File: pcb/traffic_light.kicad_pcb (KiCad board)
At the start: 2 copper layers, 30 x 130 mm, 53 parts, among them J2 Power, Q1 BS170, Q2 BS170, Q3 BS170, SW1 RESET, SW2 FLASH, U1 ESP-12F, U2 AMS1117-3.3

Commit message: laying out PCB
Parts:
- removed the REF** at (65.0, 70.0)
- removed the REF** at (65.0, 155.0)
- removed the REF** at (65.0, 77.0)
- added REF**: 1pin, istrukov:1pin_no_outline, F.Cu at (67.8, 70.0)
- added REF**: 1pin, istrukov:1pin_no_outline, F.Cu at (67.5, 155.0)
- added REF**: 1pin, istrukov:1pin_no_outline, F.Cu at (67.5, 77.0)
- moved R7 59.0 mm to (35.9, 112.0)
- moved R8 50.8 mm to (55.8, 110.8), turned to 90 degrees
- moved R12 50.0 mm to (55.8, 121.0)
- moved Q3 23.8 mm to (80.8, 169.6), turned to 90 degrees
- moved R5 23.3 mm to (54.4, 63.4), turned to 0 degrees
- moved R6 23.1 mm to (54.4, 57.4), turned to 0 degrees
- moved Q1 9.40 mm to (81.2, 61.2)
- moved R1 6.88 mm to (81.4, 67.0), turned to 0 degrees
- moved UART1 5.60 mm to (83.0, 75.2)
- moved D5 5.55 mm to (75.8, 53.6), turned to 180 degrees
- moved D6 5.40 mm to (62.4, 109.4), turned to 180 degrees
- moved D10 5.40 mm to (62.4, 122.5), turned to 180 degrees
- moved D4 5.35 mm to (75.6, 66.5), turned to 180 degrees
- moved Q2 5.15 mm to (80.4, 117.2)
- moved D1 3.00 mm to (69.2, 60.0)
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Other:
- board size 30 x 130 mm -> 35 x 130 mm

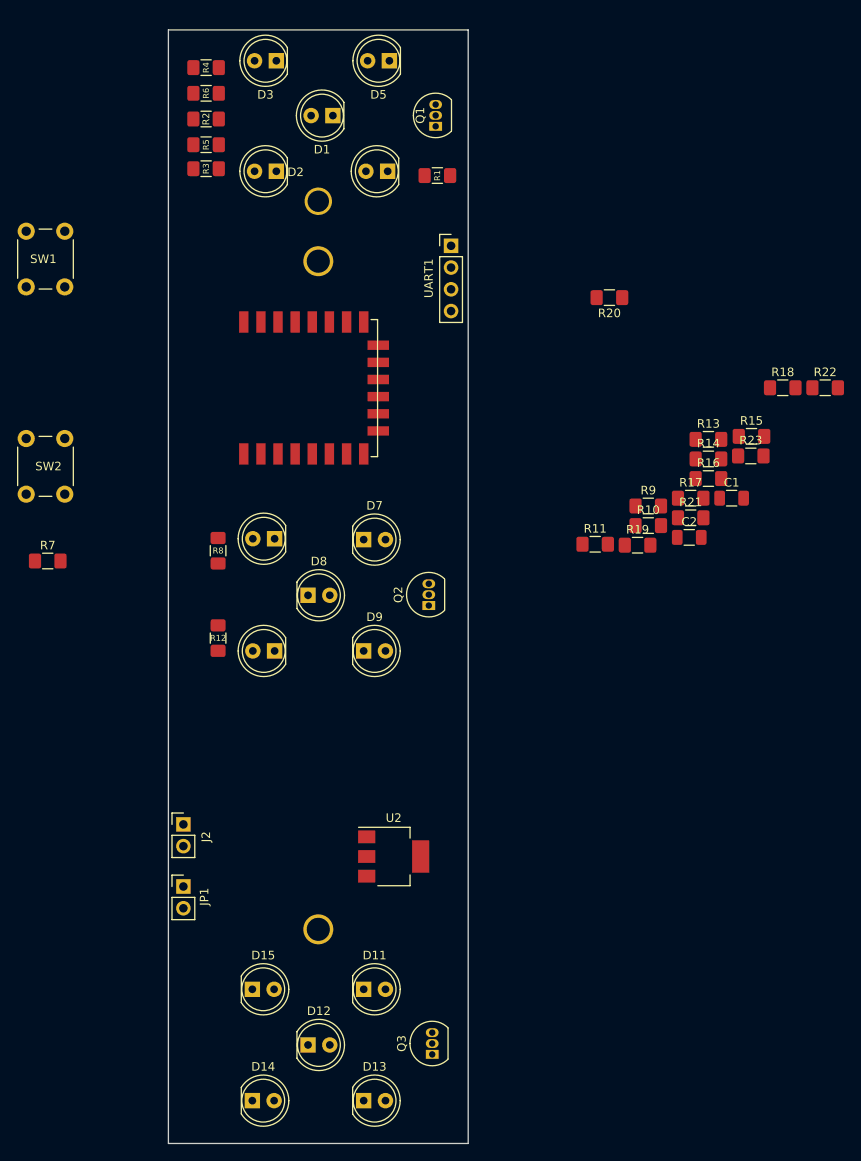
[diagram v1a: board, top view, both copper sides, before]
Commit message: place all components on the board
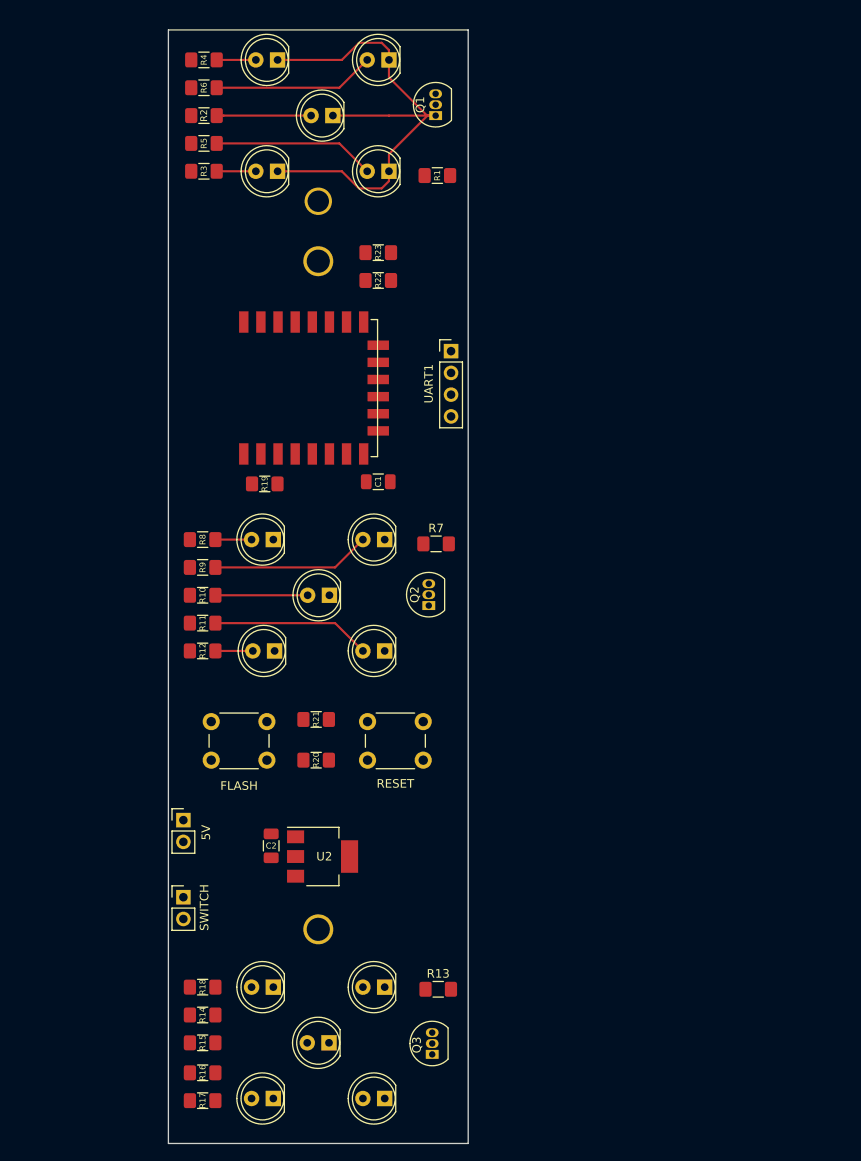
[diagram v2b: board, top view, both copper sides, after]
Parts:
- removed JP1: Power_Switch, Connector_PinHeader_2.54mm:PinHeader_1x02_P2.54mm_Vertical
- added SWITCH: Power_Switch, Connector_PinHeader_2.54mm:PinHeader_1x02_P2.54mm_Vertical, F.Cu at (51.8, 151.2)
- moved R18 97.4 mm to (54.0, 161.8)
- moved R15 95.5 mm to (54.0, 168.2)
- moved R16 91.1 mm to (54.0, 171.8)
- moved R17 90.5 mm to (54.0, 175.0)
- moved R14 87.8 mm to (54.0, 165.0)
- moved RESET 72.1 mm to (79.8, 135.2), turned to 180 degrees
- moved R13 71.5 mm to (81.5, 162.0)
- moved R20 63.9 mm to (67.2, 135.2), turned to 0 degrees
- moved C2 60.6 mm to (62.0, 145.2), turned to 90 degrees
- moved R22 53.7 mm to (74.5, 79.2)
- moved R10 52.7 mm to (54.0, 116.0)
- moved R9 52.5 mm to (54.0, 112.8)
- moved R21 49.7 mm to (67.2, 130.5), turned to 180 degrees
- moved R23 49.5 mm to (74.5, 76.0), turned to 180 degrees
- moved R11 46.7 mm to (54.0, 119.2)
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- renumbered J2 to 5V, SW2 to FLASH, SW1 to RESET
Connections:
- R10 pad 1: VCC -> +5V
- R11 pad 1: VCC -> +5V
- R12 pad 1: VCC -> +5V
- R14 pad 1: VCC -> +5V
- R15 pad 1: VCC -> +5V
- R16 pad 1: VCC -> +5V
- R17 pad 1: VCC -> +5V
- R18 pad 1: VCC -> +5V
- R2 pad 1: VCC -> +5V
- R3 pad 1: VCC -> +5V
- R4 pad 1: VCC -> +5V
- R5 pad 1: VCC -> +5V
- R6 pad 1: VCC -> +5V
- R8 pad 1: VCC -> +5V
- R9 pad 1: VCC -> +5V
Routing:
- net Net-(D1-Pad1): track 0.00 -> 61.3 mm
- net Net-(D5-Pad2): track 0.00 -> 18.9 mm
- net Net-(D4-Pad2): track 0.00 -> 18.9 mm
- net Net-(D9-Pad2): track 0.00 -> 18.6 mm
- net Net-(D7-Pad2): track 0.00 -> 18.6 mm
- net Net-(D1-Pad2): track 0.00 -> 11.0 mm
- net Net-(D8-Pad2): track 0.00 -> 10.8 mm
- net Net-(D3-Pad2): track 0.00 -> 4.57 mm
- net Net-(D2-Pad2): track 0.00 -> 4.57 mm
- net Net-(D10-Pad2): track 0.00 -> 4.37 mm
- net Net-(D6-Pad2): track 0.00 -> 4.22 mm

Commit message: route everything
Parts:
- removed 5V: Power, Connector_PinHeader_2.54mm:PinHeader_1x02_P2.54mm_Vertical
- removed FLASH: FLASH, Button_Switch_THT:SW_PUSH_6mm
- removed RESET: RESET, Button_Switch_THT:SW_PUSH_6mm
- removed SWITCH: Power_Switch, Connector_PinHeader_2.54mm:PinHeader_1x02_P2.54mm_Vertical
- added BTN1: RESET, Button_Switch_THT:SW_PUSH_6mm, F.Cu at (55.1, 130.6)
- added BTN2: FLASH, Button_Switch_THT:SW_PUSH_6mm, F.Cu at (73.4, 130.6)
- added SW1: Power_Switch, Connector_PinHeader_2.54mm:PinHeader_1x02_P2.54mm_Vertical, F.Cu at (51.9, 150.0)
- added VIN1: Power, Connector_PinHeader_2.54mm:PinHeader_1x02_P2.54mm_Vertical, F.Cu at (51.8, 142.8)
- moved R21 49.8 mm to (65.2, 80.8), turned to 0 degrees
- moved UART1 35.3 mm to (51.9, 70.8)
- moved R20 32.6 mm to (58.8, 103.8), turned to 180 degrees
- moved U2 10.7 mm to (59.4, 152.8), turned to 270 degrees
- moved R19 2.85 mm to (64.0, 103.8)
- moved C2 2.06 mm to (60.6, 146.8), turned to 0 degrees
- moved R7 1.64 mm to (80.4, 108.6)
- moved Q2 1.40 mm to (80.5, 115.8)
- moved Q3 1.35 mm to (80.8, 168.2)
- moved R13 1.00 mm to (80.5, 162.0)
- moved C1 0.30 mm to (74.2, 102.7)
- moved R16 0.25 mm to (54.0, 171.5)
- moved R17 0.25 mm to (54.0, 174.8)
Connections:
- UART1 pad 3: Net-(U1-Pad16) -> Net-(U1-Pad15)
- UART1 pad 4: Net-(U1-Pad15) -> Net-(U1-Pad16)
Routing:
- net +5V: track 0.00 -> 132.3 mm, vias 0 -> 2
- net VCC: track 0.00 -> 128.6 mm, vias 0 -> 2
- net /GREEN: track 0.00 -> 74.1 mm, vias 0 -> 2
- net /FLASH: track 0.00 -> 68.3 mm, vias 0 -> 2
- net Net-(D11-Pad1): track 0.00 -> 55.7 mm
- net Net-(D10-Pad1): track 0.00 -> 55.0 mm
- net /RED: track 0.00 -> 53.3 mm, vias 0 -> 2
- net /RST: track 0.00 -> 33.3 mm, vias 0 -> 1
- net /YELLOW: track 0.00 -> 28.0 mm, vias 0 -> 2
- net Net-(D13-Pad2): track 0.00 -> 18.6 mm
- net Net-(D11-Pad2): track 0.00 -> 18.6 mm
- net Net-(U1-Pad15): track 0.00 -> 14.2 mm
- net Net-(U1-Pad16): track 0.00 -> 11.3 mm
- net Net-(R23-Pad2): track 0.00 -> 11.0 mm
- net Net-(D12-Pad2): track 0.00 -> 10.7 mm
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- added copper zone on B.Cu, net GND
- added copper zone on F.Cu, net GND
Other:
- net class Power added: clearance 0.4, trace_width 0.5, via_dia 0.8, via_drill 0.4
- board text added: "FLASH"
- board text added: "RESET"
- board text added: "Traffic Light v1 Ilya Strukov"

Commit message: minor layout changes
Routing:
- net /RST: track 33.3 -> 39.8 mm
- net /FLASH: track 68.3 -> 74.3 mm
- net Net-(D13-Pad2): track 18.6 -> 20.0 mm
- net Net-(D9-Pad2): track 18.6 -> 20.0 mm
- net Net-(D11-Pad2): track 18.6 -> 19.9 mm
- net Net-(D4-Pad2): track 18.9 -> 20.2 mm
- net Net-(D5-Pad2): track 18.9 -> 20.1 mm
- net +5V: track 132.3 -> 133.5 mm
- net GND: vias 0 -> 2

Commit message: final touches
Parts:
- added C3: 10uF, Capacitor_SMD:C_1206_3216Metric, F.Cu at (57.0, 145.7)
- C2: value 22uF -> 10uF
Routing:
- net +5V: track 133.5 -> 134.7 mm
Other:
- board text added: "+3.3V"
- board text added: "GND"
- board text added: "RX"
- board text added: "TX"
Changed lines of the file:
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@@
   (general
     (thickness 1.6)
-    (drawings 7)
-    (tracks 213)
+    (drawings 11)
+    (tracks 214)
     (zones 0)
-    (modules 53)
+    (modules 54)
     (nets 33)
   )
@@
     (visible_elements FFFFFF7F)
     (pcbplotparams
-      (layerselection 0x010fc_ffffffff)
-      (usegerberextensions false)
+      (layerselection 0x010f0_ffffffff)
+      (usegerberextensions true)
       (usegerberattributes false)
       (usegerberadvancedattributes false)
@@
       (viasonmask false)
       (mode 1)
-      (useauxorigin false)
+      (useauxorigin true)
       (hpglpennumber 1)
       (hpglpenspeed 20)
@@
       (plotinvisibletext false)
       (padsonsilk false)
-      (subtractmaskfromsilk false)
+      (subtractmaskfromsilk true)
       (outputformat 1)
       (mirror false)
-      (drillshape 1)
+      (drillshape 0)
       (scaleselection 1)
-      (outputdirectory ""))
+      (outputdirectory "gerbers/"))
   )
   (net 0 "")
@@
       (effects (font (size 0.7 0.7) (thickness 0.1)))
     )
-    (fp_text value 22uF (at 0 1.82) (layer F.Fab)
+    (fp_text value 10uF (at 0 1.82) (layer F.Fab)
       (effects (font (size 1 1) (thickness 0.15)))
     )
@@
     (descr "Through hole straight pin header, 1x04, 2.54mm pitch, single row")
     (tags "Through hole pin header THT 1x04 2.54mm single row")
-    (fp_text reference UART1 (at 2.45 3.8 90) (layer F.SilkS)
+    (fp_text reference UART1 (at 0.7 10.45 180) (layer F.SilkS)
       (effects (font (size 1 1) (thickness 0.15)))
     )
@@
       (rotate (xyz 0 0 0))
     )
+  )
+  (module Capacitor_SMD:C_1206_3216Metric (layer F.Cu)
+    (at 56.95 145.65 90)
+    (descr "Capacitor SMD 1206 (3216 Metric), square (rectangular) end terminal, IPC_7351 nominal, (Body size source: http://www.tortai-tech.com/upload/download/2011102023233369053.pdf), generated with kicad-footprint-generator")
+    (tags capacitor)
+    (attr smd)
+    (fp_text reference C3 (at 0 -1.82 90) (layer F.SilkS)
+      (effects (font (size 1 1) (thickness 0.15)))
+    )
+    (fp_text value 10uF (at 0 1.82 90) (layer F.Fab)
+      (effects (font (size 1 1) (thickness 0.15)))
+    )
+    (fp_line (start -1.6 0.8) (end -1.6 -0.8) (layer F.Fab) (width 0.1))
+    (fp_line (start -1.6 -0.8) (end 1.6 -0.8) (layer F.Fab) (width 0.1))
+    (fp_line (start 1.6 -0.8) (end 1.6 0.8) (layer F.Fab) (width 0.1))
+    (fp_line (start 1.6 0.8) (end -1.6 0.8) (layer F.Fab) (width 0.1))
+    (fp_line (start -0.602064 -0.91) (end 0.602064 -0.91) (layer F.SilkS) (width 0.12))
+    (fp_line (start -0.602064 0.91) (end 0.602064 0.91) (layer F.SilkS) (width 0.12))
+    (fp_line (start -2.28 1.12) (end -2.28 -1.12) (layer F.CrtYd) (width 0.05))
+    (fp_line (start -2.28 -1.12) (end 2.28 -1.12) (layer F.CrtYd) (width 0.05))
+    (fp_line (start 2.28 -1.12) (end 2.28 1.12) (layer F.CrtYd) (width 0.05))
+    (fp_line (start 2.28 1.12) (end -2.28 1.12) (layer F.CrtYd) (width 0.05))
+    (fp_text user %R (at 0 0 90) (layer F.Fab)
+      (effects (font (size 0.8 0.8) (thickness 0.12)))
+    )
+    (pad 1 smd roundrect (at -1.4 0 90) (size 1.25 1.75) (layers F.Cu F.Paste F.Mask) (roundrect_rratio 0.2)
+      (net 21 +5V))
+    (pad 2 smd roundrect (at 1.4 0 90) (size 1.25 1.75) (layers F.Cu F.Paste F.Mask) (roundrect_rratio 0.2)
+      (net 2 GND))
+    (model ${KISYS3DMOD}/Capacitor_SMD.3dshapes/C_1206_3216Metric.wrl
+      (at (xyz 0 0 0))
+      (scale (xyz 1 1 1))
+      (rotate (xyz 0 0 0))
+    )
+  )
+  (gr_text +3.3V (at 55.35 70.8) (layer F.SilkS)
+    (effects (font (size 1 1) (thickness 0.15)))
+  )
+  (gr_text GND (at 55.35 73.4) (layer F.SilkS)
+    (effects (font (size 1 1) (thickness 0.15)))
+  )
+  (gr_text RX (at 54.85 75.9) (layer F.SilkS)
+    (effects (font (size 1 1) (thickness 0.15)))
+  )
+  (gr_text TX (at 54.8 78.5) (layer F.SilkS)
+    (effects (font (size 1 1) (thickness 0.15)))
   )
   (gr_text "Traffic Light v1\nIlya Strukov" (at 73.95 146.65) (layer F.SilkS)
@@
   (segment (start 52.5125 116) (end 52.5125 112.75) (width 0.5) (layer F.Cu) (net 21))
   (segment (start 52.5125 112.75) (end 52.5125 109.5) (width 0.5) (layer F.Cu) (net 21))
-  (segment (start 52.5125 153.2025) (end 51.85 152.54) (width 0.5) (layer F.Cu) (net 21))
-  (segment (start 52.5125 161.75) (end 52.5125 153.2025) (width 0.5) (layer F.Cu) (net 21))
-  (segment (start 51.85 152.54) (end 52.180002 152.54) (width 0.5) (layer F.Cu) (net 21))
-  (segment (start 52.180002 152.54) (end 53.7 151.020002) (width 0.5) (layer F.Cu) (net 21))
   (segment (start 52.5125 168.25) (end 52.5125 171.5) (width 0.5) (layer F.Cu) (net 21))
   (segment (start 52.5125 174.75) (end 52.5125 171.5) (width 0.5) (layer F.Cu) (net 21))
@@
   (segment (start 59 102.1) (end 59 72.75) (width 0.5) (layer B.Cu) (net 21))
   (segment (start 54 107.1) (end 59 102.1) (width 0.5) (layer B.Cu) (net 21))
-  (segment (start 55.070002 149.65) (end 57.1 149.65) (width 0.5) (layer F.Cu) (net 21))
-  (segment (start 53.7 151.020002) (end 55.070002 149.65) (width 0.5) (layer F.Cu) (net 21))
-  (segment (start 52.5 122.5125) (end 52.5125 122.5) (width 0.5) (layer F.Cu) (net 21))
-  (segment (start 52.5 138.75) (end 52.5 122.5125) (width 0.5) (layer F.Cu) (net 21))
-  (segment (start 55.1 141.35) (end 52.5 138.75) (width 0.5) (layer F.Cu) (net 21))
-  (segment (start 55.1 149.620002) (end 55.1 141.35) (width 0.5) (layer F.Cu) (net 21))
-  (segment (start 53.7 151.020002) (end 55.1 149.620002) (width 0.5) (layer F.Cu) (net 21))
+  (segment (start 56.95 149.5) (end 57.1 149.65) (width 0.5) (layer F.Cu) (net 21))
+  (segment (start 56.95 147.05) (end 56.95 149.5) (width 0.5) (layer F.Cu) (net 21))
+  (segment (start 51.85 161.0875) (end 52.5125 161.75) (width 0.5) (layer F.Cu) (net 21))
+  (segment (start 51.85 152.54) (end 51.85 161.0875) (width 0.5) (layer F.Cu) (net 21))
+  (segment (start 54.35 139.9) (end 52.5125 138.0625) (width 0.5) (layer F.Cu) (net 21))
+  (segment (start 52.5125 138.0625) (end 52.5125 122.5) (width 0.5) (layer F.Cu) (net 21))
+  (segment (start 53.052081 152.54) (end 54.35 151.242081) (width 0.5) (layer F.Cu) (net 21))
+  (segment (start 51.85 152.54) (end 53.052081 152.54) (width 0.5) (layer F.Cu) (net 21))
+  (segment (start 56.95 147.05) (end 55.975 147.05) (width 0.5) (layer F.Cu) (net 21))
+  (segment (start 54.35 147.05) (end 54.35 139.9) (width 0.5) (layer F.Cu) (net 21))
+  (segment (start 55.975 147.05) (end 54.35 147.05) (width 0.5) (layer F.Cu) (net 21))
+  (segment (start 54.35 151.242081) (end 54.35 147.05) (width 0.5) (layer F.Cu) (net 21))
   (segment (start 80.683847 66.228653) (end 79.9125 67) (width 0.25) (layer F.Cu) (net 22))
   (segment (start 82.275001 58.805001) (end 82.275001 64.637499) (width 0.25) (layer F.Cu) (net 22))
